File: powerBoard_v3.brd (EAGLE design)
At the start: 23.2 x 34.9 mm, 25 parts, among them U1 TLE2426CD

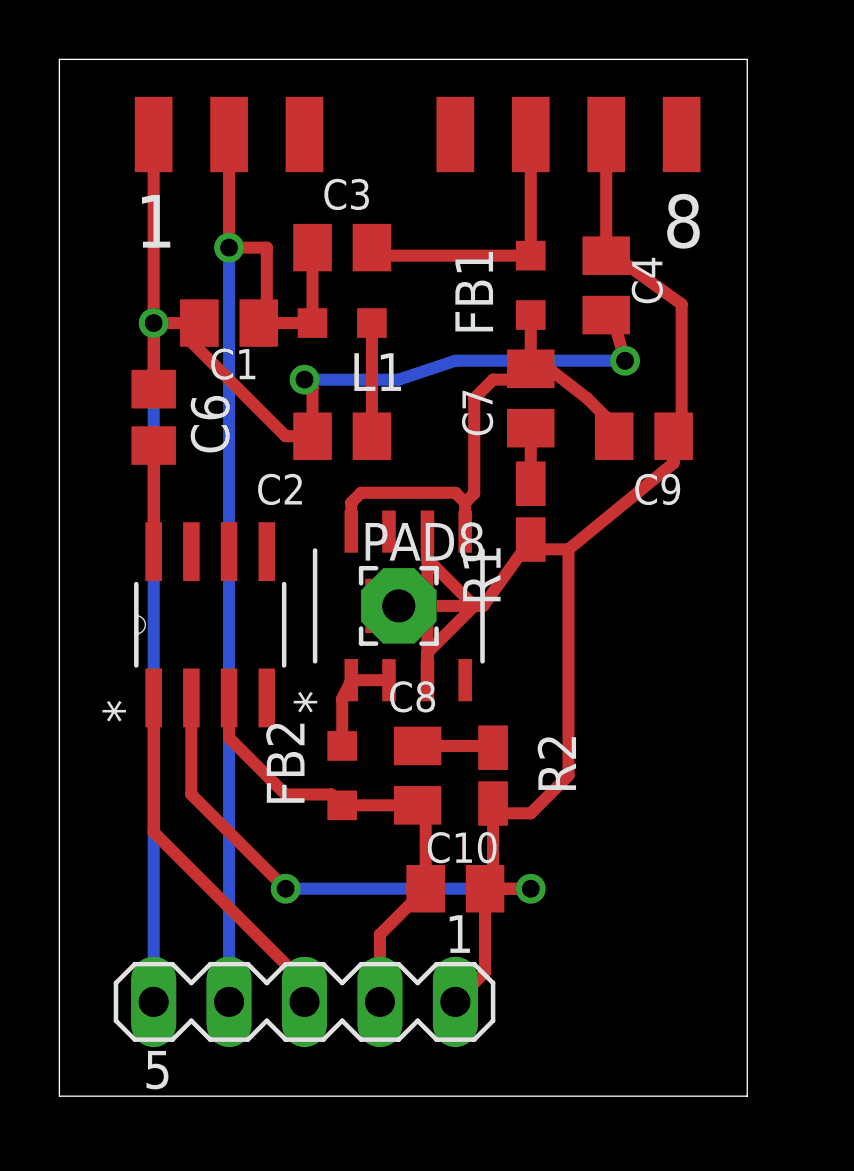
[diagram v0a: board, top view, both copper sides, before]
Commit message: updated power board designs: v2 uses low current 2.5v reference, v3 uses 10v rail and 5v ref both with simple linear regulators. Added breakout board to go from DB37 to BNC
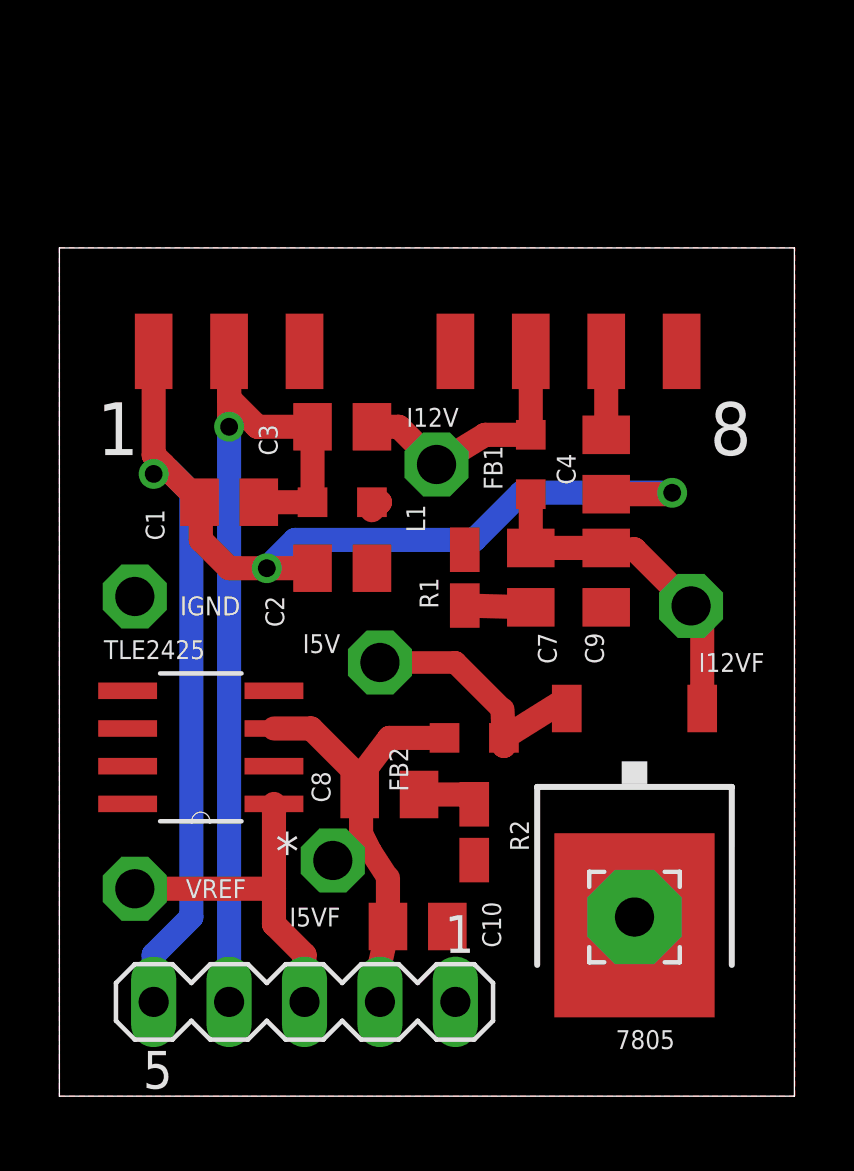
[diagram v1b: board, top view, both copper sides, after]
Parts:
- removed C6: 1uF, rcl:C0805
- removed U$1: ADP7105-REGULATOR, tuckerLib:ADP7105-REGULATOR
- removed U1: TLE2426CD, Texas Instruments_By_element14_Batch_1:SOIC127P600X175-8N
- added 7805: 7806DT, linear:TO252
- added I12V, I12VF, I5V, I5VF, IGND, VREF: PTR1PAD1-13, testpad:P1-13
- added TLE2425: TLE2425CD, Texas Instruments_By_element14_Batch_1:SOIC127P600X175-8N
- PAD8: value (none) -> WIREPAD3,17/1,3; device wirepad:2,54/1,1 -> wirepad:3,17/1,3
- moved PAD8 13.1 mm to (19.4, 6.03)
- moved PAD1 7.30 mm to (3.17, 25.1)
- moved PAD2 7.30 mm to (5.71, 25.1)
- moved PAD3 7.30 mm to (8.26, 25.1)
- moved PAD4 7.30 mm to (13.3, 25.1)
- moved PAD5 7.30 mm to (15.9, 25.1)
- moved PAD6 7.30 mm to (18.4, 25.1)
- moved PAD7 7.30 mm to (21.0, 25.1)
- moved C7 6.03 mm to (15.9, 17.5)
- moved C1 6.03 mm to (5.71, 20.0)
- moved C3 6.03 mm to (9.53, 22.5)
- moved C4 6.03 mm to (18.4, 21.3)
- moved FB1 6.03 mm to (15.9, 21.3)
- moved L1 6.03 mm to (9.53, 20.0)
- moved C9 4.93 mm to (18.4, 17.5), turned to 270 degrees
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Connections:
- removed net N$2: C6.1, U1.8
- removed net NC3: U$1.4
- removed net PG: U$1.7
- net GND: no longer C6.2
- net VREF: now also TLE2425.1, VREF.TP; no longer U1.1
- net VS1+: now also I12V.TP
- net VS1-: now also 7805.3, IGND.TP, TLE2425.2; no longer U$1.3, U$1.6, U$1.9, U1.2
- net VS1F+: now also 7805.1, I12VF.TP; no longer U$1.5, U$1.8
- net VS2+: now also 7805.2, I5V.TP; no longer U$1.1, U$1.2
- net VS2F+: now also I5VF.TP, TLE2425.3; no longer U1.3
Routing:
- net VS1-: track 72.4 -> 2.81 mm, vias 2 -> 0
- net VCC: track 37.6 -> 31.0 mm
- net VS1F+: track 17.9 -> 11.6 mm
- net GND: track 53.7 -> 47.9 mm
- net VS2+: track 3.55 -> 9.09 mm
- net N$2: track 3.57 -> 0.00 mm
- net N$1: track 4.19 -> 0.65 mm
- net VS1+: track 9.54 -> 8.97 mm
- net N$3: track 2.56 -> 1.99 mm
- net VREF: track 12.3 -> 11.8 mm
- added copper zone on layer 1, net VS1-
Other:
- board size 23.2 x 34.9 mm -> 24.8 x 28.6 mm
- board text added: "2.5V@10mA"
- board text added: "5V@200mA"
- board text added: "Sep 2016"
- board text added: "V3"
- board text added: "input: 9-18V@500mA"
- board text removed: "2.5V@300mA"
- board text removed: "5V@300mA"
- board text removed: "Aug 2016"
- board text removed: "V1"
- board text removed: "input 9-18V@1A"
